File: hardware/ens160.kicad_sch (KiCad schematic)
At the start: 6 parts, among them U8 ENS160-BGLM

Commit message: organized schem and updated readme
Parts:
- renumbered C9 to C7, C10 to C8, R17 to PR5, R18 to PR6, R15 to R7, U8 to U7
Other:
- moved on the sheet: C7, C8, PR5, PR6, R7, U7

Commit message: completed board
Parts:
- removed PR5, PR6: 4.7k, symbol Device:R
- C7, C8: footprint (none) -> Capacitor_SMD:C_1206_3216Metric_Pad1.33x1.80mm_HandSolder
- R10: renamed from R7; footprint (none) -> Resistor_SMD:R_1206_3216Metric_Pad1.30x1.75mm_HandSolder
- U7: footprint ENS160-BGLM:XDCR_ENS160-BGLM -> KML-Custom:XDCR_ENS160-BGLM
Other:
- note removed: "Pullup resistors"

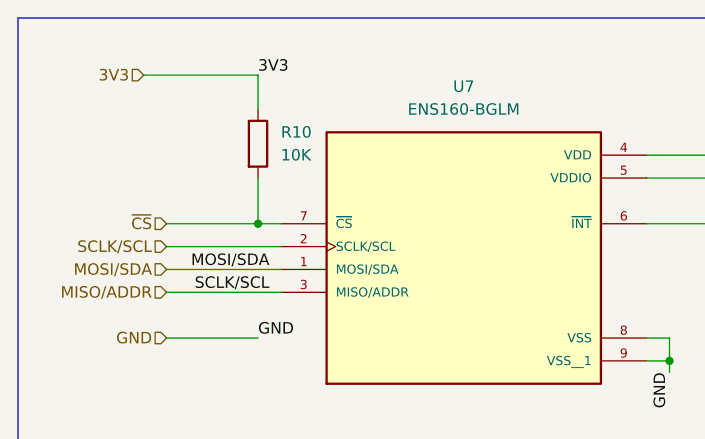
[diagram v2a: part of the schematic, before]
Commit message: final touches for order and assembly
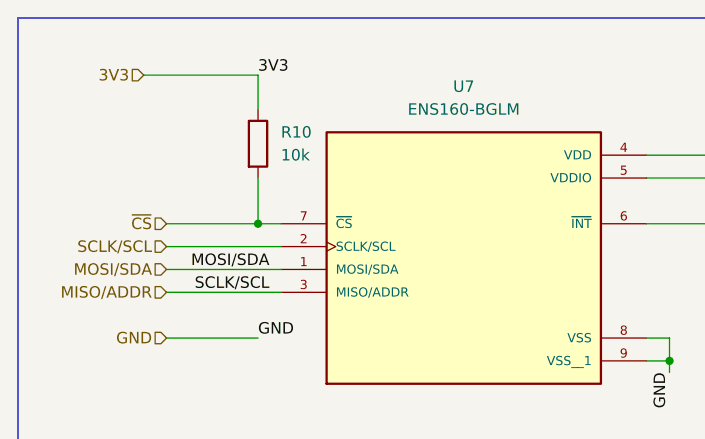
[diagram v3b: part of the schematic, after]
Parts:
- R10: value 10K -> 10k
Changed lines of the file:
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@@
 			)
 		)
-		(property "Value" "10K"
+		(property "Value" "10k"
 			(at 110.49 72.3899 0)
 			(effects
